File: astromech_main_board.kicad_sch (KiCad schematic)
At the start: 87 parts, among them IC1 MAX11645EUA+, J1 Screw_Terminal_01x02, J10 Conn_01x05, J11 Conn_01x06, J12 Conn_01x04, J13 Conn_01x05, J14 Conn_01x04, J15 Conn_01x04, J19 Conn_01x04, J2 Screw_Terminal_01x02, J20 Conn_01x04, J21 Conn_01x04, J3 Screw_Terminal_01x02, J4 IO_XPAND, J5 Conn_01x06, J6 Conn_01x06, J7 Conn_01x08, J8 Conn_01x03, J9 Conn_01x06, U1 TCA9554DW, U10 LS7366R, U11 LS7366R, U2 TCA9554DW, U3 NCP1117-3.3_SOT223, U4 NCP1117-5.0_TO252, U5 SC16IS752IPW_128, U6 TXB0108PW, U7 TCA9517ADGK, U8 74HC14, U9 LS7366R, Y1 Crystal, Y2 Crystal

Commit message: implemented suggestions
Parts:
- removed C4, C5, C6: C_Small, Capacitor_SMD:C_1206_3216Metric, symbol Device:C_Small
- removed J1, J2, J3: Screw_Terminal_01x02, astromech_footprints:PHOENIX_1984617, symbol Connector:Screw_Terminal_01x02
- removed J12: Conn_01x04, astromech_footprints:691210910004, symbol Connector_Generic:Conn_01x04
- removed R17, R8: R_Small_US, Resistor_SMD:R_1206_3216Metric, symbol Device:R_Small_US
- removed U1, U2: TCA9554DW, Package_SO:SOIC-16W_7.5x10.3mm_P1.27mm, symbol Interface_Expansion:TCA9554DW
- removed U6: TXB0108PW, Package_SO:TSSOP-20_4.4x6.5mm_P0.65mm, symbol Logic_LevelTranslator:TXB0108PW
- added J1: Conn_01x06, Connector_PinHeader_2.54mm:PinHeader_2x03_P2.54mm_Vertical, symbol Connector_Generic:Conn_01x06
- added J18: Screw_Terminal_01x10, astromech_footprints:PHOENIX_1984691, symbol Connector:Screw_Terminal_01x10
- added R7, R8: ~, Resistor_SMD:R_1206_3216Metric, symbol Device:R_US
- added U6: PCF8575PWR, astromech_footprints:SOP65P640X120-24N, symbol astromech_symbols:PCF8575PWR
- Y1: footprint Crystal:Crystal_SMD_HC49-SD_HandSoldering -> Crystal:Crystal_SMD_Abracon_ABM3-2Pin_5.0x3.2mm
- Y2: footprint Crystal:Crystal_SMD_HC49-SD_HandSoldering -> Crystal:Crystal_HC49-U_Vertical
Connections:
- net 3V3: now also R14.1, R15.1, R18.1, R19.1, J18.2 (Pin_2), U6.24 (VCC); no longer J15.1 (Pin_1), R4.1
- net 5V: now also J18.4 (Pin_4)
- net GND: now also J1.4 (Pin_4), J1.5 (Pin_5), J1.6 (Pin_6), J18.1 (Pin_1), J18.3 (Pin_3), J18.5 (Pin_5), J18.7 (Pin_7), J18.9 (Pin_9), R8.2, U6.12 (GND), U6.2 (A1), U6.21 (A0), U6.3 (A2); no longer D1.1 (K), D2.1 (K), D3.1 (K), D4.1 (K), J15.4 (Pin_4)
- net I2C_3V3_SCL: now also U6.22 (SCL)
- net I2C_3V3_SDA: now also U6.23 (SDA)
- net IO10: no longer R3.2
- net IO13: no longer U10.7 (MOSI), U11.7 (MOSI), U9.7 (MOSI)
- net IO42: now also R4.1
- net IORX: now also J14.3 (Pin_3)
- net IOTX: now also J14.2 (Pin_2)
- net RC_UART_5V: now also R7.1
- net RST: now also J1.3 (Pin_3)
- net UART_RXA: now also J15.2 (Pin_2); no longer J14.3 (Pin_3)
- net UART_RXB: now also J15.4 (Pin_4); no longer J15.3 (Pin_3)
- net UART_TXA: now also J15.1 (Pin_1); no longer J14.2 (Pin_2)
- net UART_TXB: now also J15.3 (Pin_3); no longer J15.2 (Pin_2)
- net VBAT: now also J18.6 (Pin_6)
- net at J4.1 (Pin_1): now also D1.1 (K), U6.4 (P00); no longer R19.1
- net at R19.2: now also D4.2 (A); no longer D1.2 (A)
- net at JP13.2 (C): now also R7.2, R8.1
- net at J4.3 (Pin_3): now also D3.1 (K), U6.6 (P02); no longer R15.1
- net at R15.2: now also D2.2 (A); no longer D3.2 (A)
- net at R16.2: now also J1.1 (Pin_1)
- net at J4.14 (Pin_14): now also U6.18 (P15)
- net at J4.15 (Pin_15): now also U6.19 (P16)
- net at J4.16 (Pin_16): now also U6.20 (P17)
- net at J4.9 (Pin_9): now also U6.13 (P10)
- net at J4.10 (Pin_10): now also U6.14 (P11)
- net at J4.11 (Pin_11): now also U6.15 (P12)
- net at J4.12 (Pin_12): now also U6.16 (P13)
- net at J4.13 (Pin_13): now also U6.17 (P14)
- net at J4.4 (Pin_4): now also D4.1 (K), U6.7 (P03); no longer R14.1
- net at R14.2: now also D1.2 (A); no longer D4.2 (A)
- net at F2.1: now also J18.8 (Pin_8)
- net at R18.2: now also D3.2 (A); no longer D2.2 (A)
- net at J4.6 (Pin_6): now also U6.9 (P05)
- net at J4.7 (Pin_7): now also U6.10 (P06)
- net at J4.8 (Pin_8): now also U6.11 (P07)
- net at J4.2 (Pin_2): now also D2.1 (K), U6.5 (P01); no longer R18.1
- net at J4.5 (Pin_5): now also U6.8 (P04)
- net at F1.1: now also J18.10 (Pin_10)
- removed net ENC_CNT_EN: U10.13 (CNT_EN), U11.13 (CNT_EN), U13.25 (IO_19), U9.13 (CNT_EN)
- net IO9: no longer names the net of R4.2
- net IO9: now also J1.2 (Pin_2); no longer U13.15 (IO_9)
- new net IO19: U13.25 (IO_19)
- new net IO_INT: R3.2, U13.15 (IO_9), U6.1 (~{INT})
- new net SPI_COPI: U10.7 (MOSI), U11.7 (MOSI), U9.7 (MOSI)
- no-connect marks 36 -> 39
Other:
- note added: "Encoder interrupt"
- note added: "IO expander interrupt"
- note removed: "Encoder (control pins)"
- note removed: "I2C Address: 0100001"
- note removed: "IO expander interrupt pins"
- moved on the sheet: C1, C14, C15, C16, C17, C18, C19, C2, F1, F2, H1, H2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

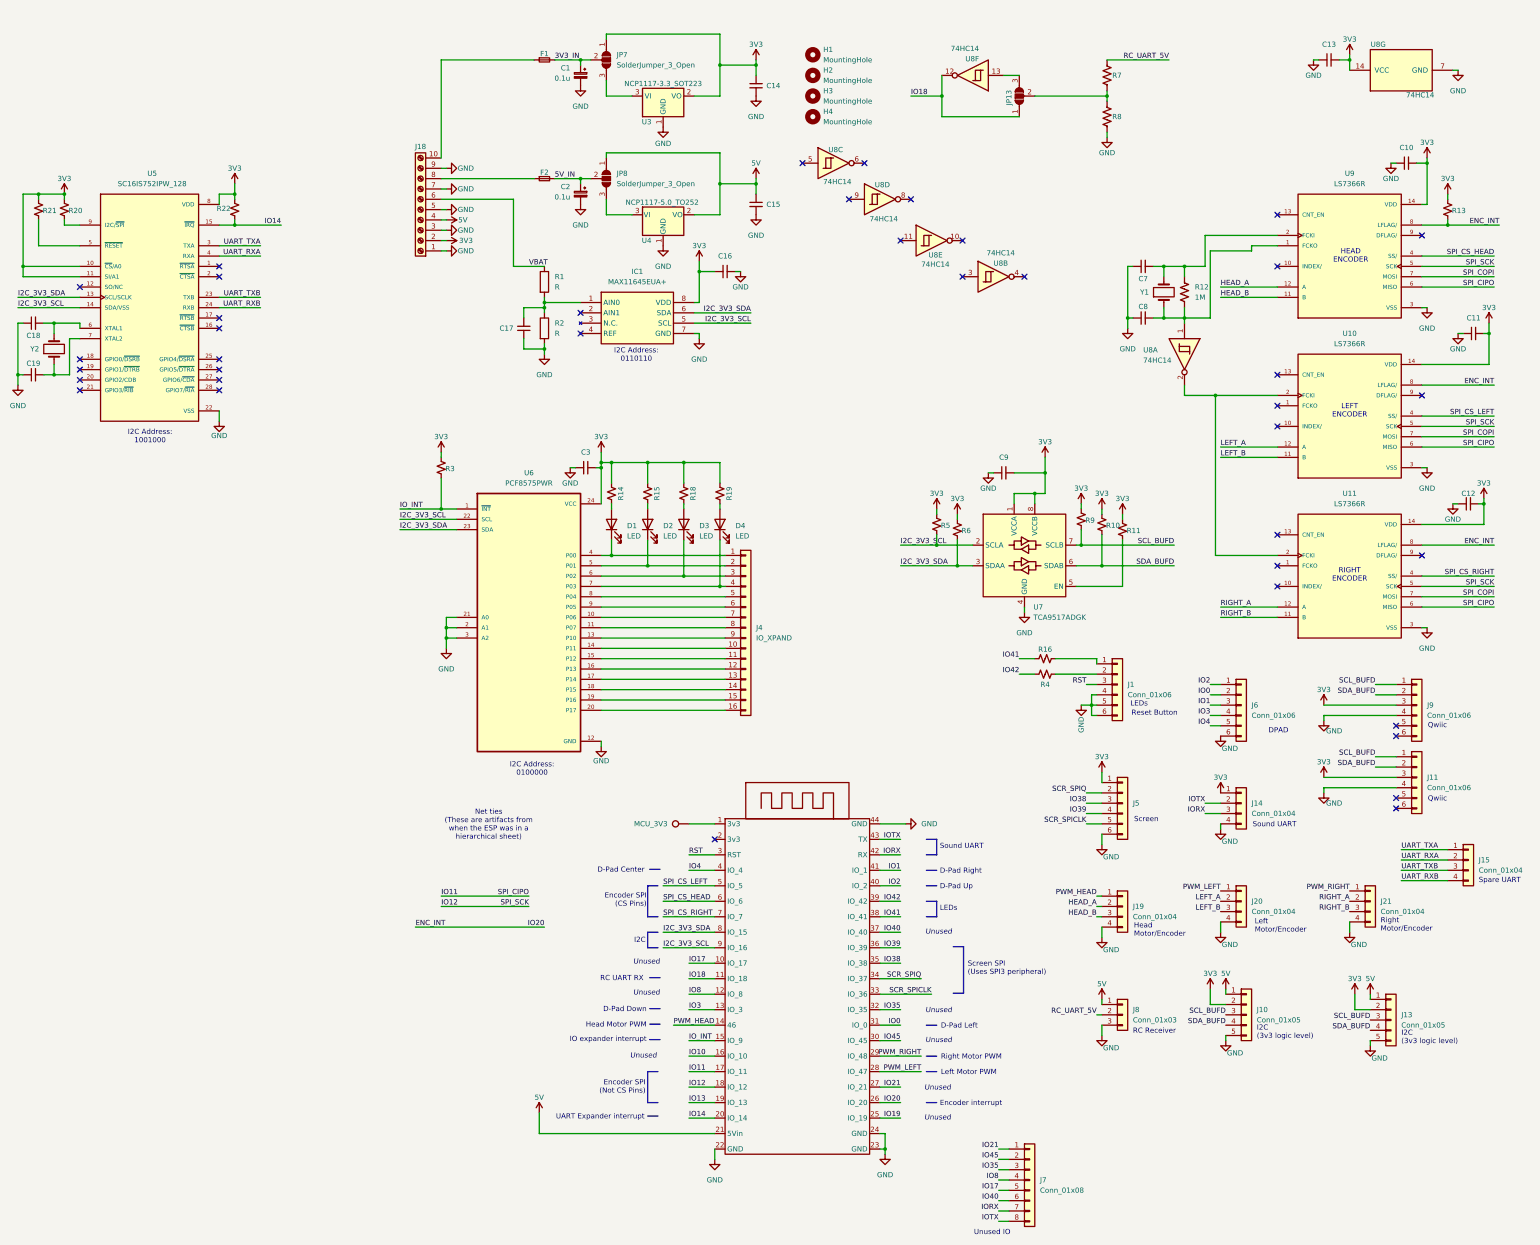
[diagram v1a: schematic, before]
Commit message: added values, 2N7002, and updated unused pins
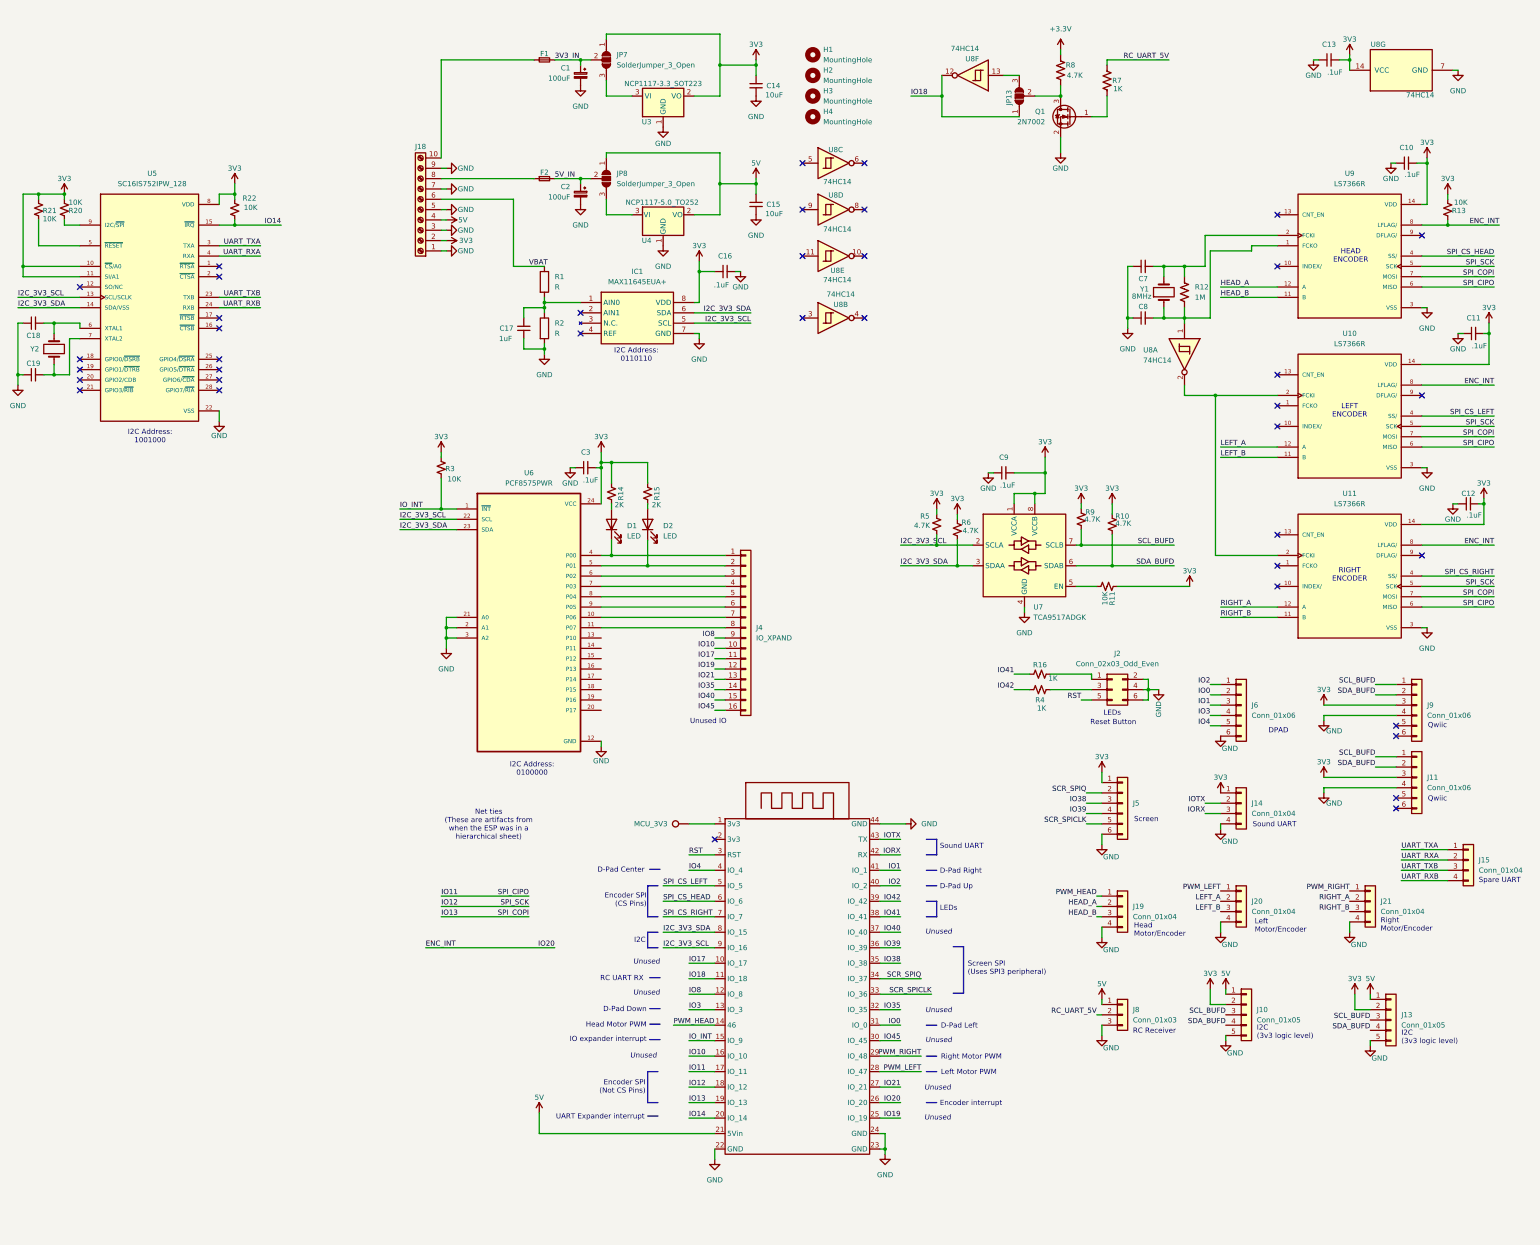
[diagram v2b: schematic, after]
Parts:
- removed D3, D4: LED, LED_SMD:LED_1206_3216Metric_Pad1.42x1.75mm_HandSolder, symbol Device:LED
- removed J1: Conn_01x06, Connector_PinHeader_2.54mm:PinHeader_2x03_P2.54mm_Vertical, symbol Connector_Generic:Conn_01x06
- removed J7: Conn_01x08, Connector_PinHeader_2.54mm:PinHeader_1x08_P2.54mm_Vertical, symbol Connector_Generic:Conn_01x08
- removed R18, R19: R_Small_US, Resistor_SMD:R_1206_3216Metric, symbol Device:R_Small_US
- added J2: Conn_02x03_Odd_Even, Connector_PinHeader_2.54mm:PinHeader_2x03_P2.54mm_Vertical, symbol Connector_Generic:Conn_02x03_Odd_Even
- added Q1: 2N7002, Package_TO_SOT_SMD:SOT-23, symbol Transistor_FET:2N7002
- C1, C2: value 0.1u -> 100uF
- C10, C11, C12, C13, C16, C3, C9: value C_Small -> .1uF
- C14, C15: value C_Small -> 10uF
- C17: value C_Small -> 1uF
- R10, R5, R6, R9: value R_Small_US -> 4.7K
- R11, R13, R20, R21, R22, R3: value R_Small_US -> 10K
- R14, R15: value R_Small_US -> 2K
- R16, R4: value R_Small_US -> 1K
- R7: value ~ -> 1K
- R8: value ~ -> 4.7K
- Y1: value Crystal -> 8MHz
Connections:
- net SPI_COPI is gone; now on net IO13: U10.7 (MOSI), U11.7 (MOSI), U9.7 (MOSI)
- net GND: now also J2.2 (Pin_2), J2.4 (Pin_4), J2.6 (Pin_6), Q1.2 (S); no longer R8.2
- net I2C_3V3_SCL: now also U5.13 (SCL/SCLK); no longer U5.14 (SDA/VSS)
- net I2C_3V3_SDA: now also U5.14 (SDA/VSS); no longer U5.13 (SCL/SCLK)
- net IO10: now also J4.10 (Pin_10)
- net IO17: now also J4.11 (Pin_11)
- net IO19: now also J4.12 (Pin_12)
- net IO21: now also J4.13 (Pin_13)
- net IO35: now also J4.14 (Pin_14)
- net IO40: now also J4.15 (Pin_15)
- net IO45: now also J4.16 (Pin_16)
- net IO8: now also J4.9 (Pin_9)
- net RST: now also J2.5 (Pin_5)
- net at R4.2: now also J2.3 (Pin_3)
- net at R16.2: now also J2.1 (Pin_1)
- net at U6.13 (P10): no longer J4.9 (Pin_9)
- net at U6.14 (P11): no longer J4.10 (Pin_10)
- net at U6.15 (P12): no longer J4.11 (Pin_11)
- net at U6.16 (P13): no longer J4.12 (Pin_12)
- net at U6.17 (P14): no longer J4.13 (Pin_13)
- net at U6.18 (P15): no longer J4.14 (Pin_14)
- net at U6.19 (P16): no longer J4.15 (Pin_15)
- net at U6.20 (P17): no longer J4.16 (Pin_16)
- new net: JP13.2 (C), Q1.3 (D), R8.2
- new net: Q1.1 (G), R7.2
- new net +3.3V: R8.1
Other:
- moved on the sheet: R10, R11, R16, R4, R7, U8B, U8D, U8E
